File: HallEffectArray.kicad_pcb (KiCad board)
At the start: 2 copper layers, 101.6 x 101.6 mm, 47 parts, among them J1 Conn_01x06_Female, U1 DRV5055, U2 DRV5055, U3 DRV5055, U4 DRV5055, U5 DRV5055, U6 DRV5055, U7 DRV5055, U8 DRV5055, U9 LM324

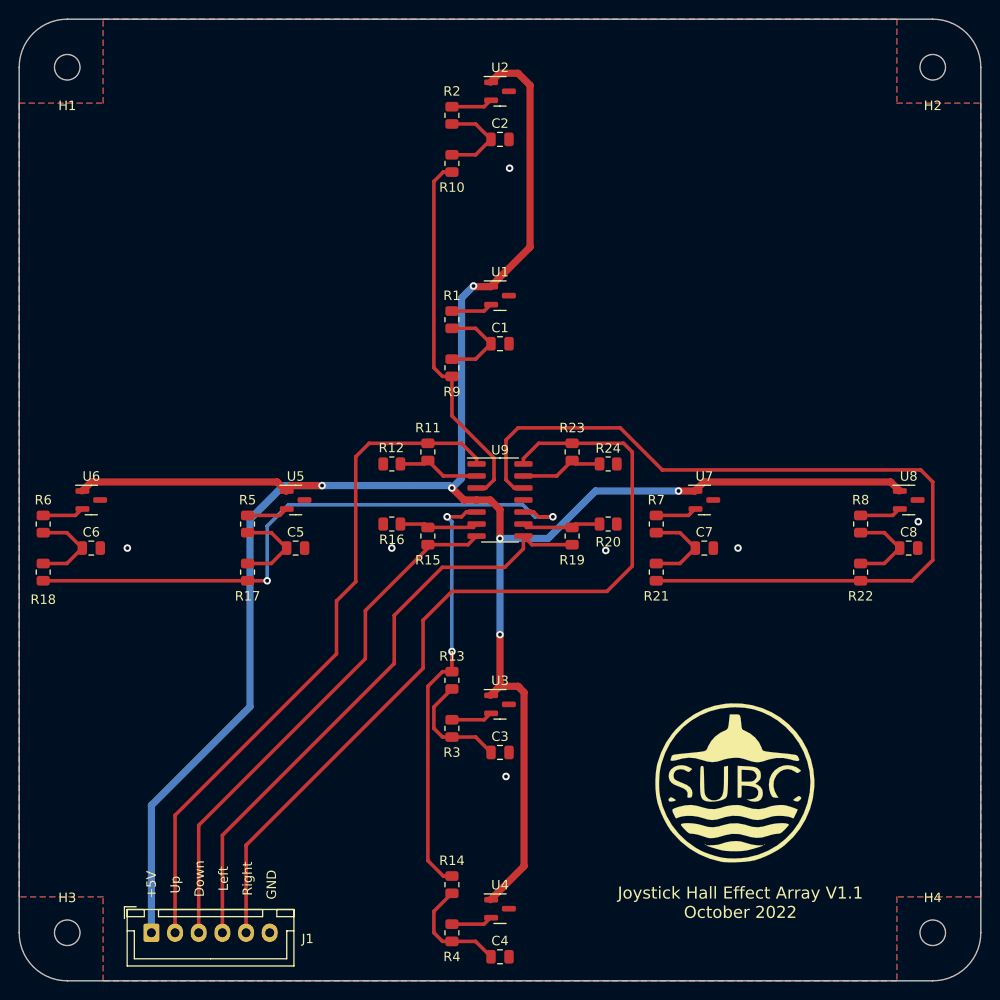
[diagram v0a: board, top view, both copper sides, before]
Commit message: Version 1.2: Added trimmer pots, bypass capacitors, vias, board size now 100x100mm
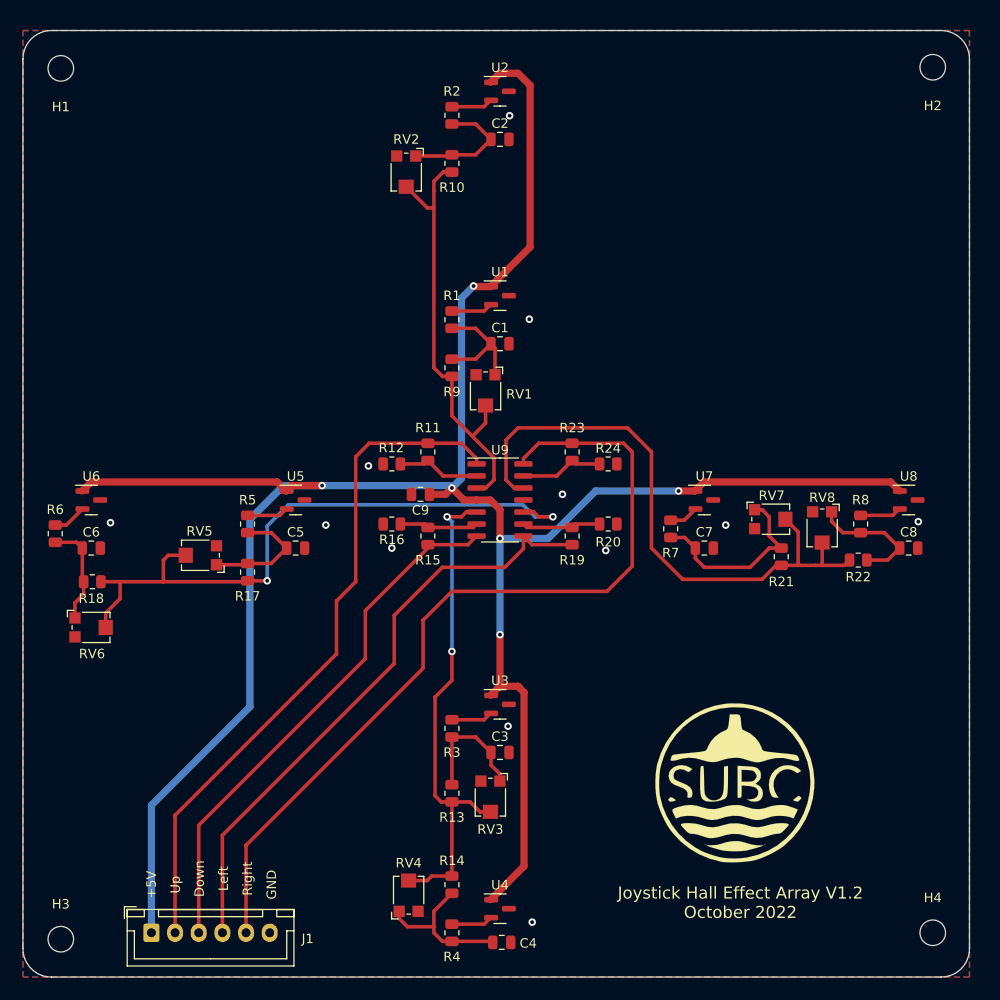
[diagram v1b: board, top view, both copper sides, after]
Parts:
- added C9: 100nF, Capacitor_SMD:C_0805_2012Metric, F.Cu at (144.0, 101.0)
- added RV1: 10k, Potentiometer_SMD:Potentiometer_Bourns_TC33X_Vertical, F.Cu at (150.9, 90.2)
- added RV2: 10k, Potentiometer_SMD:Potentiometer_Bourns_TC33X_Vertical, F.Cu at (142.5, 67.1)
- added RV3: 10k, Potentiometer_SMD:Potentiometer_Bourns_TC33X_Vertical, F.Cu at (151.4, 133.1)
- added RV4: 10k, Potentiometer_SMD:Potentiometer_Bourns_TC33X_Vertical, F.Cu at (142.7, 143.3)
- added RV5: 10k, Potentiometer_SMD:Potentiometer_Bourns_TC33X_Vertical, F.Cu at (120.7, 107.4)
- added RV6: 10k, Potentiometer_SMD:Potentiometer_Bourns_TC33X_Vertical, F.Cu at (109.3, 115.1)
- added RV7: 10k, Potentiometer_SMD:Potentiometer_Bourns_TC33X_Vertical, F.Cu at (181.1, 103.6)
- added RV8: 10k, Potentiometer_SMD:Potentiometer_Bourns_TC33X_Vertical, F.Cu at (186.4, 104.6)
- moved R21 13.3 mm to (182.1, 107.6)
- moved R13 11.9 mm to (147.3, 132.6), turned to 90 degrees
- moved R18 5.28 mm to (109.3, 110.2), turned to 180 degrees
- moved R6 1.63 mm to (105.4, 105.2)
- moved R7 1.61 mm to (170.4, 104.6)
- moved C4 1.54 mm to (152.6, 148.3)
- moved R22 1.30 mm to (190.2, 108.0), turned to 0 degrees
- moved H3 0.96 mm to (106.0, 148.0)
- moved H1 0.69 mm to (106.0, 56.0)
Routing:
- net Net-(R21-Pad1): track 92.8 -> 64.5 mm
- net Hall7Out: track 9.61 -> 20.1 mm
- net Net-(R13-Pad1): track 44.7 -> 52.9 mm
- net Net-(R10-Pad1): track 39.2 -> 46.9 mm
- net Hall4Out: track 12.0 -> 16.4 mm
- net Net-(R17-Pad1): track 64.4 -> 68.7 mm
- net Hall2Out: track 9.61 -> 13.5 mm
- net Hall8Out: track 9.61 -> 13.4 mm
- net Hall1Out: track 9.61 -> 13.1 mm
- net Hall5Out: track 9.61 -> 12.9 mm
- net +5V: track 247.4 -> 250.0 mm
- net Hall6Out: track 9.61 -> 10.9 mm
- net Net-(R7-Pad1): track 4.36 -> 3.11 mm
- net Hall3Out: track 12.0 -> 13.3 mm
- net Net-(R6-Pad1): track 4.36 -> 3.57 mm
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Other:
- board size 101.6 x 101.6 mm -> 100 x 100 mm
- board text added: "Joystick Hall Effect Array V1.2 October 2022"
- board text removed: "Joystick Hall Effect Array V1.1 October 2022"

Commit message: V1.3: Added decoupling caps on outputs, more vias, changed datasheet
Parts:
- added C10: 100nF, Capacitor_SMD:C_0805_2012Metric, F.Cu at (130.6, 120.0)
- added C11: 10uF, Capacitor_SMD:C_0805_2012Metric, F.Cu at (130.5, 116.0)
- added C12: 100nF, Capacitor_SMD:C_0805_2012Metric, F.Cu at (134.5, 120.0)
- added C13: 10uF, Capacitor_SMD:C_0805_2012Metric, F.Cu at (134.5, 116.0)
- added C14: 100nF, Capacitor_SMD:C_0805_2012Metric, F.Cu at (138.5, 120.0)
- added C15: 10uF, Capacitor_SMD:C_0805_2012Metric, F.Cu at (138.5, 116.0)
- added C16: 100nF, Capacitor_SMD:C_0805_2012Metric, F.Cu at (142.5, 120.0)
- added C17: 10uF, Capacitor_SMD:C_0805_2012Metric, F.Cu at (142.5, 116.0)
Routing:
- net Right: track 90.4 -> 92.8 mm
- net Left: track 64.5 -> 66.2 mm
- net Down: track 56.5 -> 58.3 mm
- net GND: vias 12 -> 30
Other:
- board text added: "Joystick Hall Effect Array V1.3 November 2022"
- board text removed: "Joystick Hall Effect Array V1.2 October 2022"
